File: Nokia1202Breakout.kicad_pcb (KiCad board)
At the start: 2 copper layers, 36.8 x 47.5 mm, 6 parts, among them J1 Conn_01x08_Male

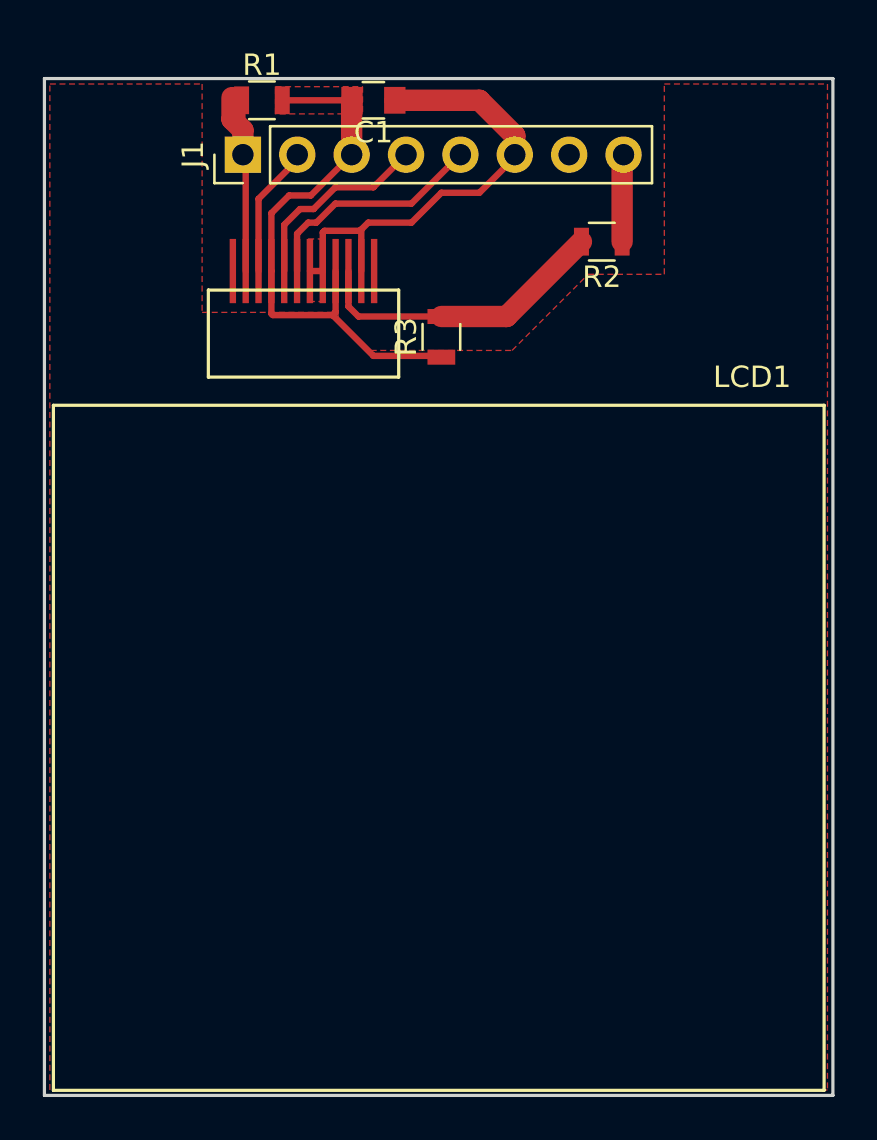
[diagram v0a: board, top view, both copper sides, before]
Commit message: Fixed incorrect reset connection.
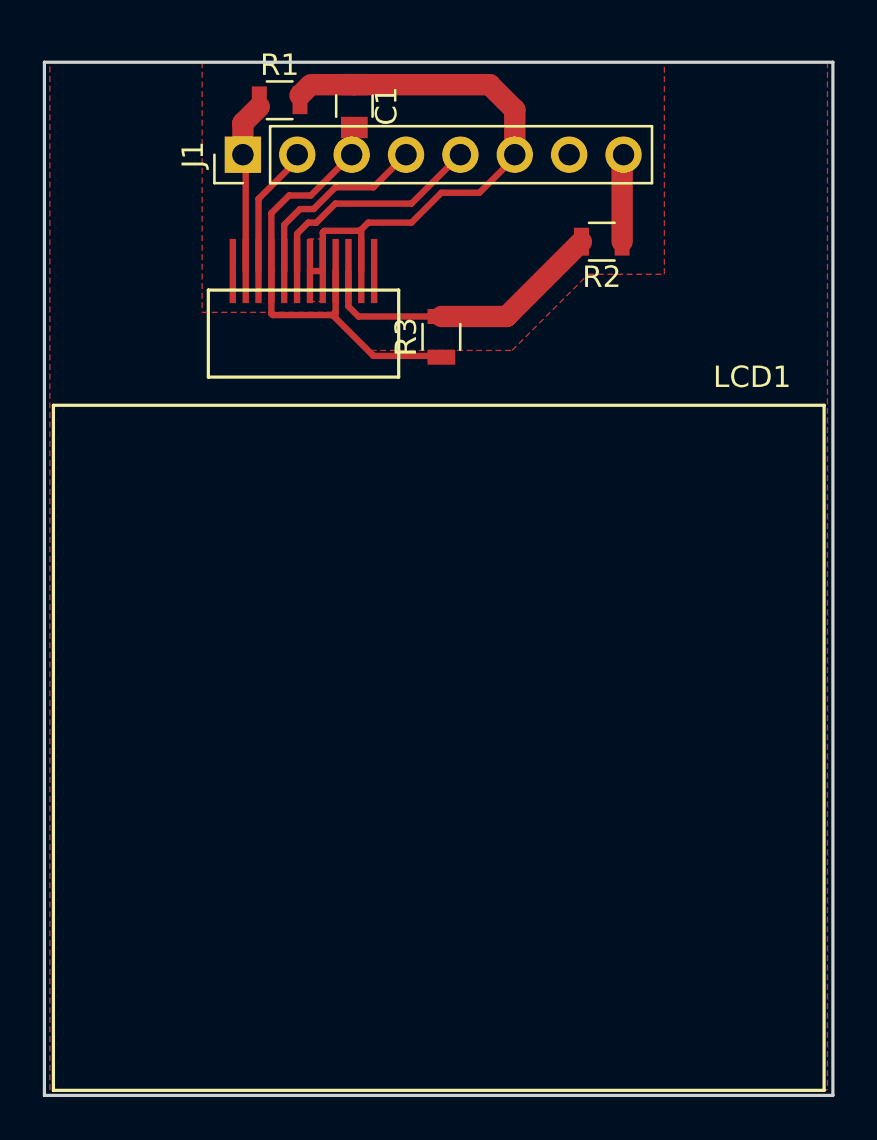
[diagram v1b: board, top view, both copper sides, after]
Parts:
- moved C1 0.93 mm to (29.5, 14.7), turned to 270 degrees
- moved R1 0.83 mm to (26.0, 14.5)
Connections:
- R1 pad 2: Net-(C1-Pad2) -> Net-(C1-Pad1)
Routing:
- net Net-(C1-Pad2): track 28.8 -> 21.8 mm
- net Net-(C1-Pad1): track 22.1 -> 27.9 mm
- net Net-(J1-Pad1): track 10.9 -> 8.35 mm
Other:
- board size 36.8 x 47.5 mm -> 36.8 x 48.3 mm
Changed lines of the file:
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@@
     (links 17)
     (no_connects 0)
-    (area 14.910999 13.386999 51.891001 61.035001)
+    (area 14.910999 12.624999 51.891001 61.035001)
     (thickness 1.6)
     (drawings 4)
-    (tracks 64)
+    (tracks 63)
     (zones 0)
     (modules 6)
@@
   )
   (setup
-    (last_trace_width 0.25)
+    (last_trace_width 1)
     (user_trace_width 0.3)
     (user_trace_width 0.4)
@@
   )
   (module Capacitors_SMD:C_0805 (layer F.Cu)
-    (at 30.353 14.478 180)
+    (at 29.464 14.748 270)
     (descr "Capacitor SMD 0805, reflow soldering, AVX (see smccp.pdf)")
     (tags "capacitor 0805")
     (attr smd)
-    (fp_text reference C1 (at 0 -1.5 180) (layer F.SilkS)
-      (effects (font (size 1 1) (thickness 0.15)))
-    )
-    (fp_text value 0.1uF (at 0 1.75 180) (layer F.Fab)
-      (effects (font (size 1 1) (thickness 0.15)))
-    )
-    (fp_text user %R (at 0 -1.5 180) (layer F.Fab)
+    (fp_text reference C1 (at 0 -1.5 270) (layer F.SilkS)
+      (effects (font (size 1 1) (thickness 0.15)))
+    )
+    (fp_text value 0.1uF (at 0 1.75 270) (layer F.Fab)
+      (effects (font (size 1 1) (thickness 0.15)))
+    )
+    (fp_text user %R (at 0 -1.5 270) (layer F.Fab)
       (effects (font (size 1 1) (thickness 0.15)))
     )
@@
     (fp_line (start 1.75 0.87) (end 1.75 -0.88) (layer F.CrtYd) (width 0.05))
     (fp_line (start 1.75 0.87) (end -1.75 0.87) (layer F.CrtYd) (width 0.05))
-    (pad 1 smd rect (at -1 0 180) (size 1 1.25) (layers F.Cu F.Paste F.Mask)
-      (net 1 "Net-(C1-Pad1)"))
-    (pad 2 smd rect (at 1 0 180) (size 1 1.25) (layers F.Cu F.Paste F.Mask)
+    (pad 1 smd rect (at -1 0 270) (size 1 1.25) (layers F.Cu F.Paste F.Mask)
+      (net 1 "Net-(C1-Pad1)"))
+    (pad 2 smd rect (at 1 0 270) (size 1 1.25) (layers F.Cu F.Paste F.Mask)
       (net 2 "Net-(C1-Pad2)"))
     (model Capacitors_SMD.3dshapes/C_0805.wrl
@@
   )
   (module Resistors_SMD:R_0805 (layer F.Cu)
-    (at 25.146 14.478)
+    (at 25.974 14.478)
     (descr "Resistor SMD 0805, reflow soldering, Vishay (see dcrcw.pdf)")
     (tags "resistor 0805")
@@
       (net 3 "Net-(J1-Pad1)"))
     (pad 2 smd rect (at 0.95 0) (size 0.7 1.3) (layers F.Cu F.Paste F.Mask)
-      (net 2 "Net-(C1-Pad2)"))
+      (net 1 "Net-(C1-Pad1)"))
     (model ${KISYS3DMOD}/Resistors_SMD.3dshapes/R_0805.wrl
       (at (xyz 0 0 0))
@@
   )
   (gr_line (start 51.816 60.96) (end 14.986 60.96) (angle 90) (layer Edge.Cuts) (width 0.15))
-  (gr_line (start 14.986 13.462) (end 14.986 60.96) (angle 90) (layer Edge.Cuts) (width 0.15))
-  (gr_line (start 51.816 13.462) (end 14.986 13.462) (angle 90) (layer Edge.Cuts) (width 0.15))
-  (gr_line (start 51.816 60.96) (end 51.816 13.462) (angle 90) (layer Edge.Cuts) (width 0.15))
-  (segment (start 31.353 14.478) (end 35.306 14.478) (width 1) (layer F.Cu) (net 1))
-  (segment (start 36.957 16.129) (end 36.957 17.018) (width 1) (layer F.Cu) (net 1))
-  (segment (start 35.306 14.478) (end 36.957 16.129) (width 1) (layer F.Cu) (net 1))
+  (gr_line (start 14.986 12.7) (end 14.986 60.96) (angle 90) (layer Edge.Cuts) (width 0.15))
+  (gr_line (start 51.816 12.7) (end 14.986 12.7) (angle 90) (layer Edge.Cuts) (width 0.15))
+  (gr_line (start 51.816 60.96) (end 51.816 12.7) (angle 90) (layer Edge.Cuts) (width 0.15))
+  (segment (start 35.782 13.748) (end 36.957 14.923) (width 1) (layer F.Cu) (net 1))
+  (segment (start 36.957 14.923) (end 36.957 17.018) (width 1) (layer F.Cu) (net 1))
+  (segment (start 29.464 13.748) (end 35.782 13.748) (width 1) (layer F.Cu) (net 1))
+  (segment (start 26.924 14.478) (end 26.924 14.25) (width 0.25) (layer F.Cu) (net 1))
+  (segment (start 26.924 14.25) (end 27.426 13.748) (width 1) (layer F.Cu) (net 1))
+  (segment (start 27.686 13.748) (end 29.464 13.748) (width 1) (layer F.Cu) (net 1))
+  (segment (start 27.426 13.748) (end 27.686 13.748) (width 0.25) (layer F.Cu) (net 1))
   (segment (start 36.957 17.018) (end 36.957 17.145) (width 0.25) (layer F.Cu) (net 1))
   (segment (start 36.957 17.145) (end 35.306 18.796) (width 0.3) (layer F.Cu) (net 1))
@@
   (segment (start 28.067 20.574) (end 27.9871 20.6539) (width 0.3) (layer F.Cu) (net 1))
   (segment (start 27.3871 22.4536) (end 27.9871 22.4536) (width 0.3) (layer F.Cu) (net 1))
-  (segment (start 26.096 14.478) (end 29.353 14.478) (width 0.3) (layer F.Cu) (net 2))
-  (segment (start 29.353 14.478) (end 29.337 14.494) (width 1) (layer F.Cu) (net 2))
-  (segment (start 29.337 14.494) (end 29.337 17.018) (width 1) (layer F.Cu) (net 2))
-  (segment (start 29.337 14.494) (end 29.337 17.018) (width 0.25) (layer F.Cu) (net 2))
+  (segment (start 29.337 17.018) (end 29.337 15.875) (width 0.25) (layer F.Cu) (net 2))
+  (segment (start 29.337 15.875) (end 29.464 15.748) (width 0.25) (layer F.Cu) (net 2))
   (segment (start 28.448 24.511) (end 30.353 26.416) (width 0.3) (layer F.Cu) (net 2))
   (segment (start 30.353 26.416) (end 33.467 26.416) (width 0.3) (layer F.Cu) (net 2))
   (segment (start 33.467 26.416) (end 33.528 26.477) (width 0.25) (layer F.Cu) (net 2))
-  (segment (start 29.353 14.478) (end 29.337 14.494) (width 0.25) (layer F.Cu) (net 2))
   (segment (start 25.5871 22.4536) (end 25.5871 19.7519) (width 0.3) (layer F.Cu) (net 2))
   (segment (start 27.432 18.923) (end 29.337 17.018) (width 0.3) (layer F.Cu) (net 2))
@@
   (segment (start 28.5871 24.3719) (end 28.5871 22.4536) (width 0.3) (layer F.Cu) (net 2))
   (segment (start 28.448 24.511) (end 28.5871 24.3719) (width 0.3) (layer F.Cu) (net 2))
-  (segment (start 24.257 17.018) (end 24.257 15.875) (width 1) (layer F.Cu) (net 3))
-  (segment (start 23.749 15.367) (end 23.749 14.351) (width 1) (layer F.Cu) (net 3))
-  (segment (start 24.257 15.875) (end 23.749 15.367) (width 1) (layer F.Cu) (net 3))
-  (segment (start 24.257 17.018) (end 24.257 14.539) (width 0.25) (layer F.Cu) (net 3))
-  (segment (start 24.257 14.539) (end 24.196 14.478) (width 0.25) (layer F.Cu) (net 3))
+  (segment (start 24.257 17.018) (end 24.257 15.545) (width 1) (layer F.Cu) (net 3))
+  (segment (start 24.257 15.545) (end 25.024 14.778) (width 1) (layer F.Cu) (net 3))
+  (segment (start 25.024 14.778) (end 25.024 14.478) (width 0.25) (layer F.Cu) (net 3))
   (segment (start 24.3871 22.4536) (end 24.3871 17.1481) (width 0.3) (layer F.Cu) (net 3))
   (segment (start 24.3871 17.1481) (end 24.257 17.018) (width 0.25) (layer F.Cu) (net 3))
@@
   (segment (start 41.971 17.084) (end 42.037 17.018) (width 1) (layer F.Cu) (net 11))
   (segment (start 41.971 17.084) (end 42.037 17.018) (width 0.25) (layer F.Cu) (net 11))
-  (zone (net 2) (net_name "Net-(C1-Pad2)") (layer F.Cu) (hatch edge 0.508)
-    (connect_pads yes (clearance 0))
-    (min_thickness 0.1)
-    (fill yes (arc_segments 16) (thermal_gap 0.508) (thermal_bridge_width 0.508))
-    (polygon
-      (pts
-        (xy 25.781 13.843) (xy 29.845 13.843) (xy 29.845 15.113) (xy 25.781 15.113)
-      )
-    )
-  )
   (zone (net 1) (net_name "Net-(C1-Pad1)") (layer F.Cu) (hatch edge 0.508)
     (connect_pads yes (clearance 0))
@@
   (zone (net 2) (net_name "Net-(C1-Pad2)") (layer F.Cu) (hatch edge 0.508)
     (connect_pads yes (clearance 0))
-    (min_thickness 0.1)
+    (min_thickness 0.254)
     (fill yes (arc_segments 16) (thermal_gap 0.508) (thermal_bridge_width 0.508))
     (polygon
       (pts
         (xy 22.352 24.384) (xy 28.702 24.384) (xy 28.702 24.638) (xy 30.226 26.162) (xy 36.83 26.162)
-        (xy 40.386 22.606) (xy 43.942 22.606) (xy 43.942 13.716) (xy 51.562 13.716) (xy 51.562 60.706)
-        (xy 15.24 60.706) (xy 15.24 13.716) (xy 22.352 13.716)
+        (xy 40.386 22.606) (xy 43.942 22.606) (xy 43.942 12.7) (xy 51.562 12.7) (xy 51.562 60.706)
+        (xy 15.24 60.706) (xy 15.24 12.7) (xy 22.352 12.7)
       )
     )

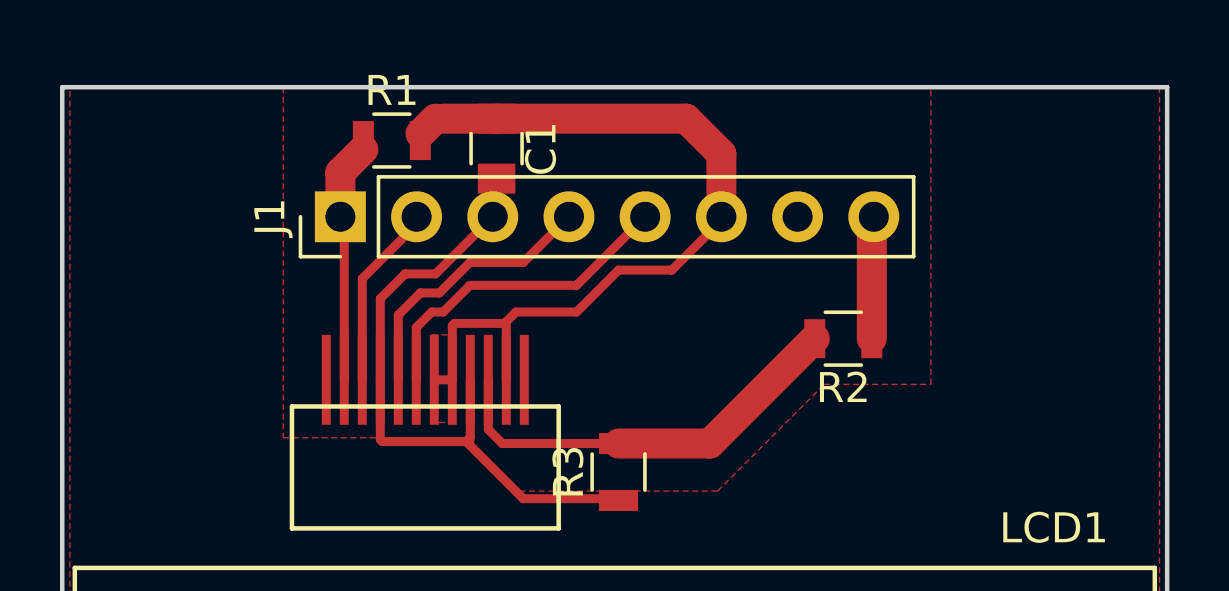
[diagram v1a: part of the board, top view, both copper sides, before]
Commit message: Added mounting holes, prepared negative copies for photochemical printing.
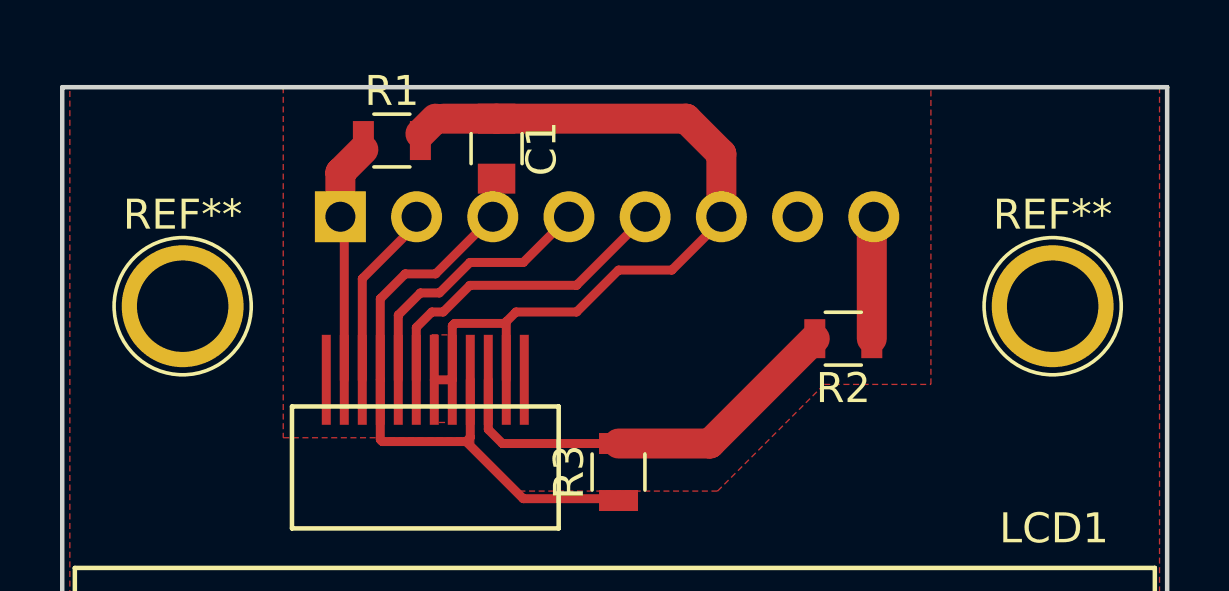
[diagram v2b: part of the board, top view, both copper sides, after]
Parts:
- added REF**: 1pin, Connectors:1pin, F.Cu at (48.0, 20.0)
- added REF**: 1pin, Connectors:1pin, F.Cu at (19.0, 20.0)
- J1: footprint Pin_Headers:Pin_Header_Straight_1x08_Pitch2.54mm -> Pin_Headers:Pin_Header_Angled_1x08_Pitch2.54mm; moved to B.Cu
- turned J1 to 270 degrees
